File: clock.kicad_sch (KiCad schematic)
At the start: 52 parts, among them J1 USB_C_Receptacle_USB2.0_16P, J3 Conn_01x02_Pin, J4 Conn_01x02_Pin, J5 Battery, Q1 NMOS-SI2302, Q2 NPN, SW1 SW_SPST, SW2 SW_SPST, SW4 SW_SPDT, SW5 SW_SPST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

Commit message: changed it ig
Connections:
- net +3.3V: now also BZ1.1 (+)
- net BUZZER: now also R13.1; no longer BZ1.1 (+)
- net GND: now also Q2.3 (E); no longer BZ1.2 (-)
- net at D1.2 (A), Q2.1 (C): now also BZ1.2 (-)
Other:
- moved on the sheet: BZ1
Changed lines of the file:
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@@
 	(global_label "BUZZER"
 		(shape input)
-		(at 257.81 87.63 180)
+		(at 224.79 90.17 180)
 		(fields_autoplaced yes)
 		(effects
@@
 		)
 		(property "Intersheetrefs" "${INTERSHEET_REFS}"
-			(at 247.3863 87.63 0)
+			(at 214.3663 90.17 0)
 			(effects
 				(font
@@
 	(symbol
 		(lib_id "Device:Buzzer")
-		(at 260.35 90.17 0)
+		(at 246.38 81.28 0)
 		(unit 1)
 		(exclude_from_sim no)
@@
 		(fields_autoplaced yes)
 		(property "Reference" "BZ1"
-			(at 264.16 88.8999 0)
+			(at 250.19 80.0099 0)
 			(effects
 				(font
@@
 		)
 		(property "Value" "Buzzer"
-			(at 264.16 91.4399 0)
+			(at 250.19 82.5499 0)
 			(effects
 				(font
@@
 		)
 		(property "Footprint" "Buzzer_Beeper:MagneticBuzzer_CUI_CMT-8504-100-SMT"
-			(at 259.715 87.63 90)
+			(at 245.745 78.74 90)
 			(effects
 				(font
@@
 		)
 		(property "Datasheet" "~"
-			(at 259.715 87.63 90)
+			(at 245.745 78.74 90)
 			(effects
 				(font
@@
 		)
 		(property "Description" "Buzzer, polarized"
-			(at 260.35 90.17 0)
+			(at 246.38 81.28 0)
 			(effects
 				(font
@@
 	(symbol
 		(lib_id "power:GND")
-		(at 257.81 92.71 270)
+		(at 240.03 95.25 0)
 		(unit 1)
 		(exclude_from_sim no)
@@
 		(fields_autoplaced yes)
 		(property "Reference" "#PWR09"
-			(at 251.46 92.71 0)
+			(at 240.03 101.6 0)
 			(effects
 				(font
@@
 		)
 		(property "Value" "GND"
-			(at 256.54 88.9 90)
+			(at 242.57 96.5199 0)
 			(effects
 				(font
 					(size 1.27 1.27)
 				)
+				(justify left)
 			)
 		)
 		(property "Footprint" ""
-			(at 257.81 92.71 0)
+			(at 240.03 95.25 0)
 			(effects
 				(font
@@
 		)
 		(property "Datasheet" ""
-			(at 257.81 92.71 0)
+			(at 240.03 95.25 0)
 			(effects
 				(font
@@
 		)
 		(property "Description" "Power symbol creates a global label with name \"GND\" , ground"
-			(at 257.81 92.71 0)
+			(at 240.03 95.25 0)
 			(effects
 				(font

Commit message: idk again
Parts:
- R13: value 470R -> 180R
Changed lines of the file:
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@@
 			)
 		)
-		(property "Value" "470R"
+		(property "Value" "180R"
 			(at 228.6 86.36 90)
 			(effects

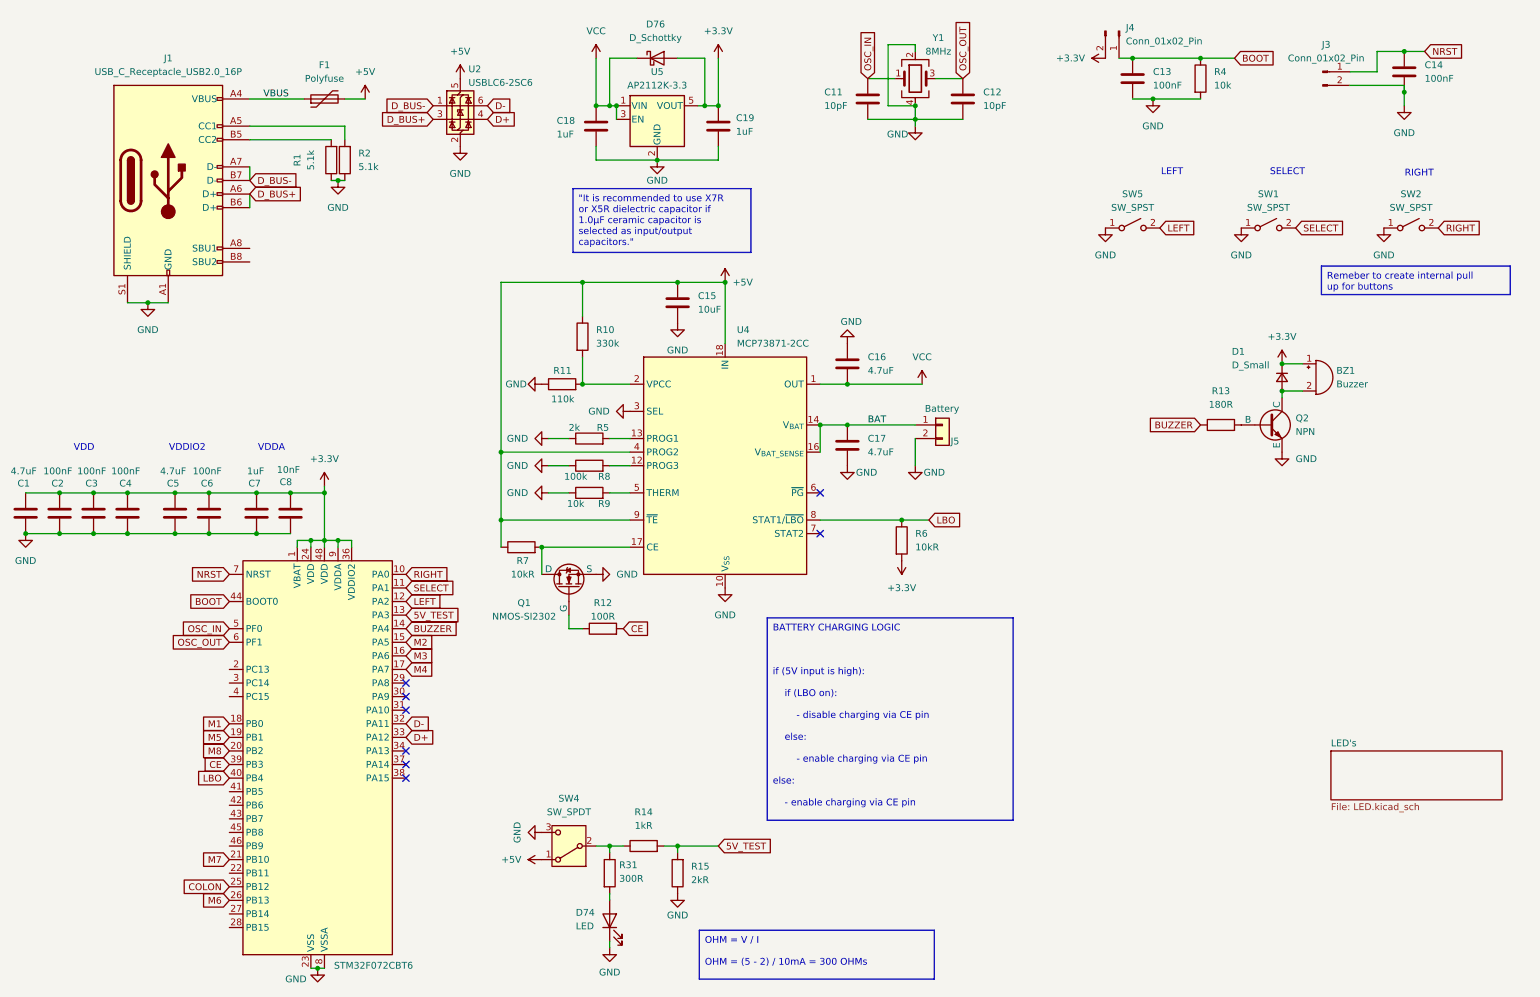
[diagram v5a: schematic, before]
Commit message: looking good, changed buzzer, changed buzzer pin, changed resistors, changed stcube ide config
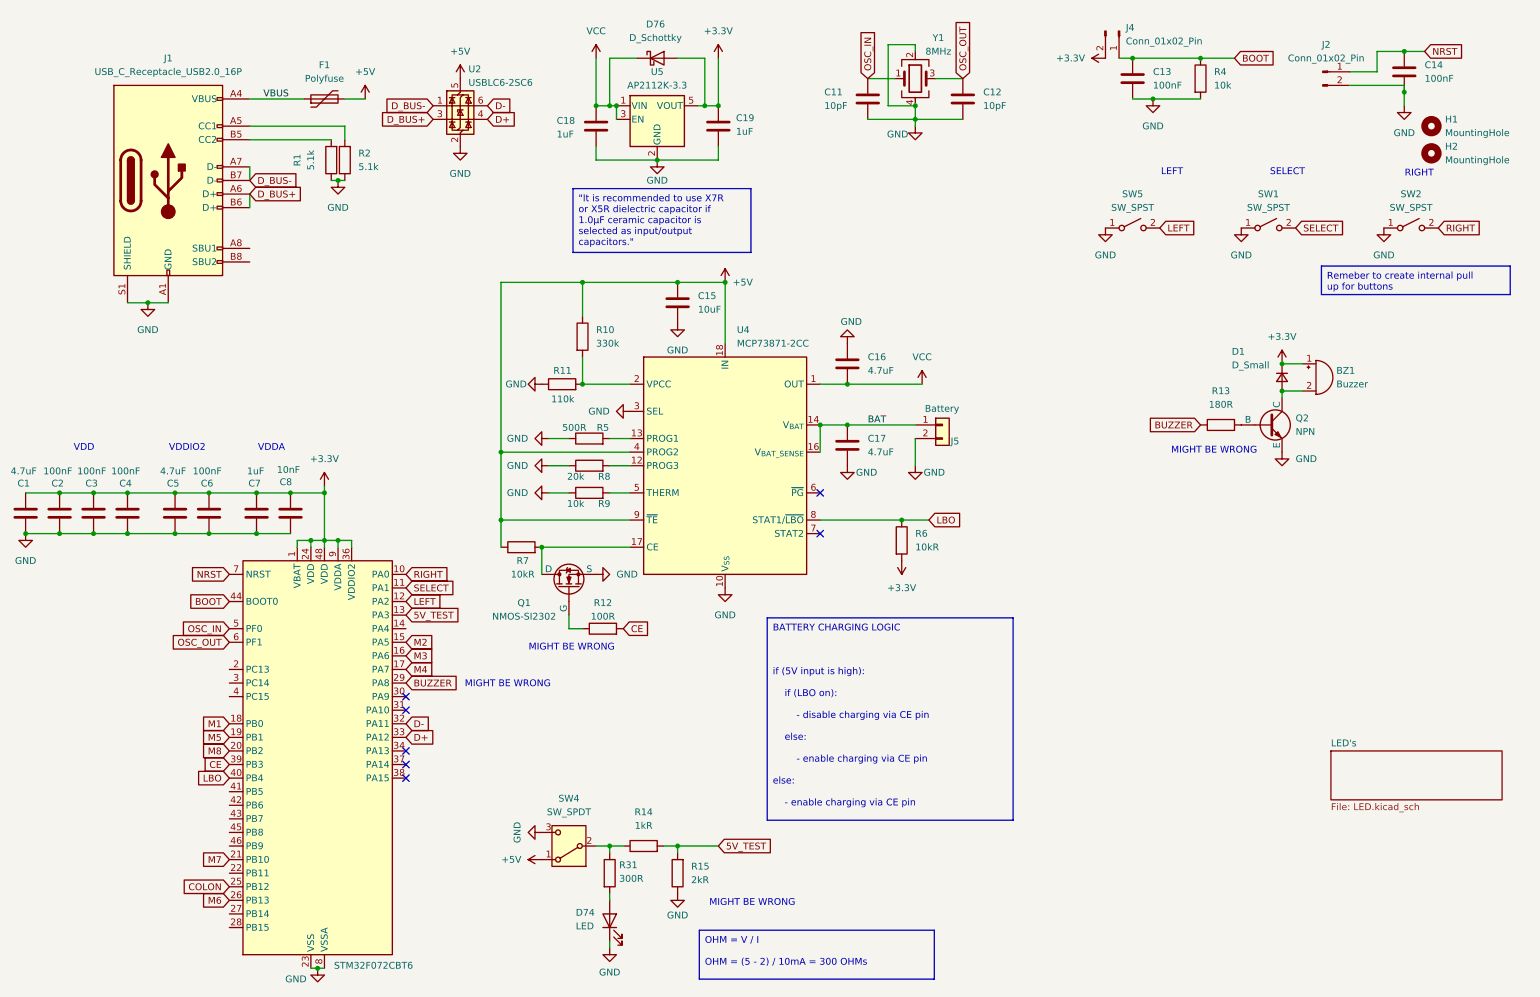
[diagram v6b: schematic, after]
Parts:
- removed J3: Conn_01x02_Pin, Connector_PinHeader_2.54mm:PinHeader_1x02_P2.54mm_Vertical, symbol Connector:Conn_01x02_Pin
- added H1, H2: MountingHole, MountingHole:MountingHole_3.2mm_M3, symbol Mechanical:MountingHole
- added J2: Conn_01x02_Pin, Connector_PinHeader_2.54mm:PinHeader_1x02_P2.54mm_Vertical, symbol Connector:Conn_01x02_Pin
- BZ1: footprint Buzzer_Beeper:MagneticBuzzer_CUI_CMT-8504-100-SMT -> FB_clock_lib:Buzzer
- R5: value 2k -> 500R
- R8: value 100k -> 20k
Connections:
- net BUZZER: now also U1.29 (PA8); no longer U1.14 (PA4)
- net GND: now also J2.2 (Pin_2)
- net NRST: now also J2.1 (Pin_1)
- no-connect marks 8 -> 7
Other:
- note added: "MIGHT BE WRONG"
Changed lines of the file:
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@@
 	)
 	(no_connect
-		(at 76.2 138.43)
-	)
-	(no_connect
 		(at 76.2 140.97)
 	)
@@
 		)
 	)
+	(text "MIGHT BE WRONG\n"
+		(exclude_from_sim no)
+		(at 227.33 94.996 0)
+		(effects
+			(font
+				(size 1.27 1.27)
+			)
+		)
+	)
 	(text "VDDA"
 		(exclude_from_sim no)
@@
 		)
 	)
+	(text "MIGHT BE WRONG\n"
+		(exclude_from_sim no)
+		(at 95.25 138.684 0)
+		(effects
+			(font
+				(size 1.27 1.27)
+			)
+		)
+	)
+	(text "MIGHT BE WRONG\n"
+		(exclude_from_sim no)
+		(at 140.97 179.578 0)
+		(effects
+			(font
+				(size 1.27 1.27)
+			)
+		)
+	)
 	(text "RIGHT"
 		(exclude_from_sim no)
@@
 		)
 	)
+	(text "MIGHT BE WRONG\n"
+		(exclude_from_sim no)
+		(at 107.188 131.826 0)
+		(effects
+			(font
+				(size 1.27 1.27)
+			)
+		)
+	)
 	(label "BAT"
 		(at 162.56 90.17 0)
-		(fields_autoplaced yes)
 		(effects
 			(font
@@
 	(label "VBUS"
 		(at 49.53 29.21 0)
-		(fields_autoplaced yes)
 		(effects
 			(font
@@
 	(global_label "BUZZER"
 		(shape input)
-		(at 76.2 128.27 0)
+		(at 76.2 138.43 0)
 		(fields_autoplaced yes)
 		(effects
@@
 		)
 		(property "Intersheetrefs" "${INTERSHEET_REFS}"
-			(at 86.6237 128.27 0)
+			(at 86.6237 138.43 0)
 			(effects
 				(font
@@
 			)
 		)
-		(property "Footprint" "Buzzer_Beeper:MagneticBuzzer_CUI_CMT-8504-100-SMT"
+		(property "Footprint" "FB_clock_lib:Buzzer"
 			(at 245.745 78.74 90)
 			(effects
@@
 			)
 		)
-		(property "Value" "2k"
+		(property "Value" "500R"
 			(at 107.696 90.678 90)
 			(effects
@@
 	)
 	(symbol
+		(lib_id "Connector:Conn_01x02_Pin")
+		(at 247.65 24.13 0)
+		(unit 1)
+		(exclude_from_sim no)
+		(in_bom yes)
+		(on_board yes)
+		(dnp no)
+		(fields_autoplaced yes)
+		(property "Reference" "J2"
+			(at 248.285 19.05 0)
+			(effects
+				(font
+					(size 1.27 1.27)
+				)
+			)
+		)
+		(property "Value" "Conn_01x02_Pin"
+			(at 248.285 21.59 0)
+			(effects
+				(font
+					(size 1.27 1.27)
+				)
+			)
+		)
+		(property "Footprint" "Connector_PinHeader_2.54mm:PinHeader_1x02_P2.54mm_Vertical"
+			(at 247.65 24.13 0)
+			(effects
+				(font
+					(size 1.27 1.27)
+				)
+				(hide yes)
+			)
+		)
+		(property "Datasheet" "~"
+			(at 247.65 24.13 0)
+			(effects
+				(font
+					(size 1.27 1.27)
+				)
+				(hide yes)
+			)
+		)
+		(property "Description" "Generic connector, single row, 01x02, script generated"
+			(at 247.65 24.13 0)
+			(effects
+				(font
+					(size 1.27 1.27)
+				)
+				(hide yes)
+			)
+		)
+		(pin "2"
+		)
+		(pin "1"
+		)
+		(instances
+			(project "clock"
+				(path "/959d2641-02eb-4caa-b1c6-84a86321825f"
+					(reference "J2")
+					(unit 1)
+				)
+			)
+		)
+	)
+	(symbol
 		(lib_id "Device:R")
 		(at 62.23 40.64 180)
@@
 			)
 		)
-		(property "Value" "100k"
+		(property "Value" "20k"
 			(at 107.95 99.822 90)
 			(effects
@@
 	)
 	(symbol
-		(lib_id "Connector:Conn_01x02_Pin")
-		(at 247.65 24.13 0)
-		(unit 1)
-		(exclude_from_sim no)
-		(in_bom yes)
-		(on_board yes)
-		(dnp no)
-		(fields_autoplaced yes)
-		(property "Reference" "J3"
-			(at 248.285 19.05 0)
-			(effects
-				(font
-					(size 1.27 1.27)
-				)
-			)
-		)
-		(property "Value" "Conn_01x02_Pin"
-			(at 248.285 21.59 0)
-			(effects
-				(font
-					(size 1.27 1.27)
-				)
-			)
-		)
-		(property "Footprint" "Connector_PinHeader_2.54mm:PinHeader_1x02_P2.54mm_Vertical"
-			(at 247.65 24.13 0)
-			(effects
-				(font
-					(size 1.27 1.27)
-				)
-				(hide yes)
-			)
-		)
-		(property "Datasheet" "~"
-			(at 247.65 24.13 0)
-			(effects
-				(font
-					(size 1.27 1.27)
-				)
-				(hide yes)
-			)
-		)
-		(property "Description" "Generic connector, single row, 01x02, script generated"
-			(at 247.65 24.13 0)
-			(effects
-				(font
-					(size 1.27 1.27)
-				)
-				(hide yes)
-			)
-		)
-		(pin "2"
-		)
-		(pin "1"
-		)
-		(instances
-			(project "clock"
-				(path "/959d2641-02eb-4caa-b1c6-84a86321825f"
-					(reference "J3")
-					(unit 1)
-				)
-			)
-		)
-	)
-	(symbol
 		(lib_id "Switch:SW_SPDT")
 		(at 106.68 168.91 180)
@@
 	)
 	(symbol
+		(lib_id "Mechanical:MountingHole")
+		(at 267.97 39.37 0)
+		(unit 1)
+		(exclude_from_sim yes)
+		(in_bom no)
+		(on_board yes)
+		(dnp no)
+		(fields_autoplaced yes)
+		(property "Reference" "H2"
+			(at 270.51 38.0999 0)
+			(effects
+				(font
+					(size 1.27 1.27)
+				)
+				(justify left)
+			)
+		)
+		(property "Value" "MountingHole"
+			(at 270.51 40.6399 0)
+			(effects
+				(font
+					(size 1.27 1.27)
+				)
+				(justify left)
+			)
+		)
+		(property "Footprint" "MountingHole:MountingHole_3.2mm_M3"
+			(at 267.97 39.37 0)
+			(effects
+				(font
+					(size 1.27 1.27)
+				)
+				(hide yes)
+			)
+		)
+		(property "Datasheet" "~"
+			(at 267.97 39.37 0)
+			(effects
+				(font
+					(size 1.27 1.27)
+				)
+				(hide yes)
+			)
+		)
+		(property "Description" "Mounting Hole without connection"
+			(at 267.97 39.37 0)
+			(effects
+				(font
+					(size 1.27 1.27)
+				)
+				(hide yes)
+			)
+		)
+		(instances
+			(project "clock"
+				(path "/959d2641-02eb-4caa-b1c6-84a86321825f"
+					(reference "H2")
+					(unit 1)
+				)
+			)
+		)
+	)
+	(symbol
 		(lib_id "power:GND")
 		(at 127 71.12 0)
@@
 					(unit 1)
 				)
+			)
+		)
+	)
+	(symbol
+		(lib_id "Mechanical:MountingHole")
+		(at 267.97 34.29 0)
+		(unit 1)
+		(exclude_from_sim yes)
+		(in_bom no)
+		(on_board yes)
+		(dnp no)
+		(fields_autoplaced yes)
+		(property "Reference" "H1"
+			(at 270.51 33.0199 0)
+			(effects
+				(font
+					(size 1.27 1.27)
+				)
+				(justify left)
+			)
+		)
+		(property "Value" "MountingHole"
+			(at 270.51 35.5599 0)
+			(effects
+				(font
+					(size 1.27 1.27)
+				)
+				(justify left)
+			)
+		)
+		(property "Footprint" "MountingHole:MountingHole_3.2mm_M3"
+			(at 267.97 34.29 0)
+			(effects
+				(font
+					(size 1.27 1.27)
+				)
+				(hide yes)
+			)
+		)
+		(property "Datasheet" "~"
+			(at 267.97 34.29 0)
+			(effects
+				(font
+					(size 1.27 1.27)
+				)
+				(hide yes)
+			)
+		)
+		(property "Description" "Mounting Hole without connection"
+			(at 267.97 34.29 0)
+			(effects
+				(font
+					(size 1.27 1.27)
+				)
+				(hide yes)
+			)
+		)
+		(instances
+			(project ""
+				(path "/959d2641-02eb-4caa-b1c6-84a86321825f"
+					(reference "H1")
+					(unit 1)
+				)

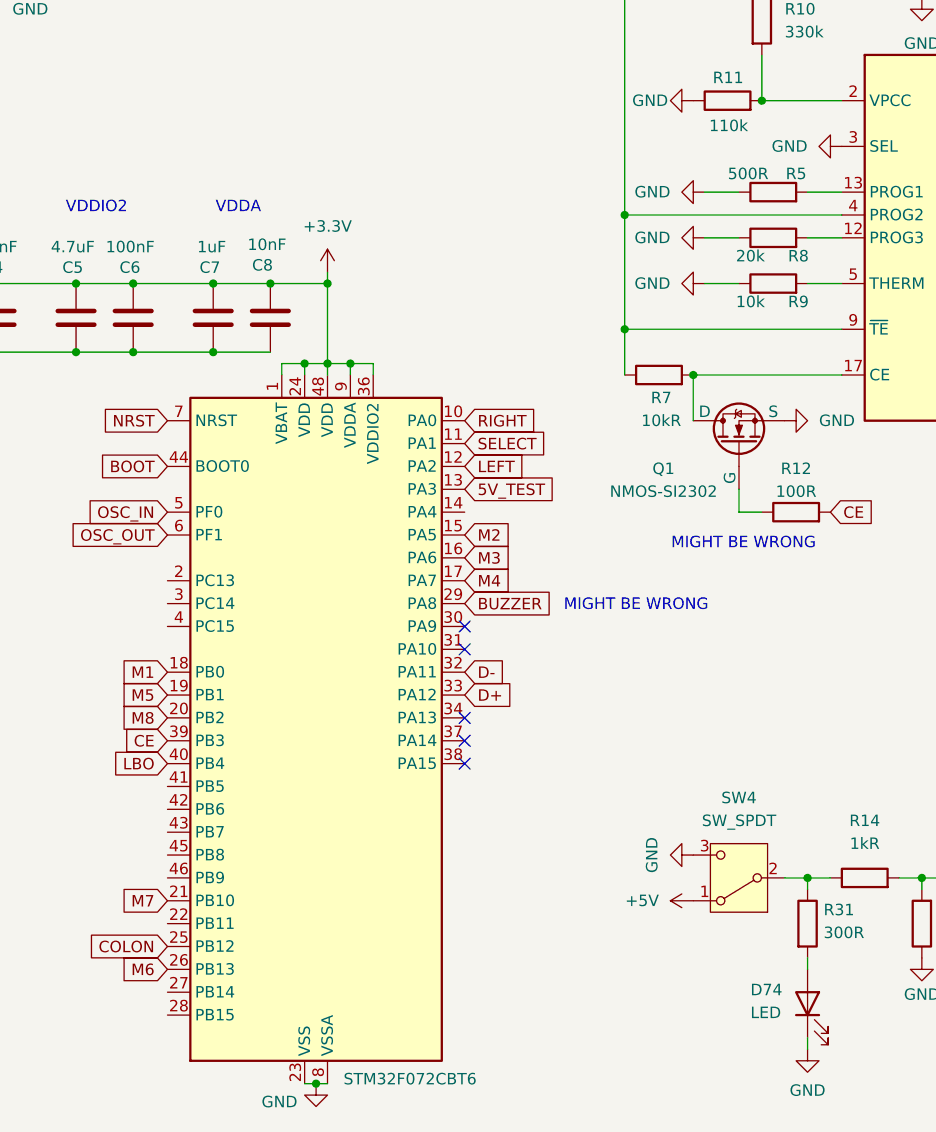
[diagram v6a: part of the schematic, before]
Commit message: changed resistor values
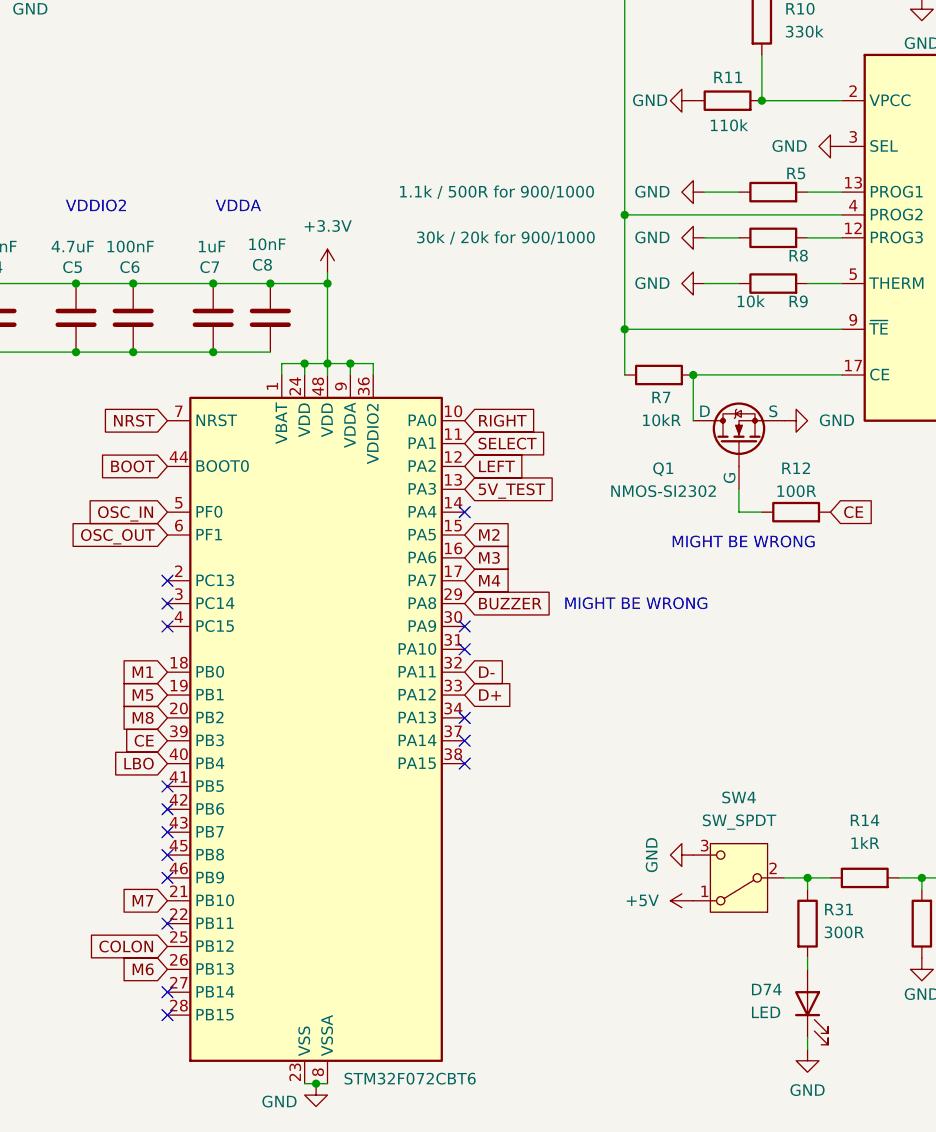
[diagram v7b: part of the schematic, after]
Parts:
- R5: value 500R -> 1.1k / 500R for 900/1000
- R8: value 20k -> 30k / 20k for 900/1000
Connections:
- no-connect marks 7 -> 19
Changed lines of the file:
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@@
 	)
 	(no_connect
+		(at 43.18 163.83)
+	)
+	(no_connect
 		(at 153.67 102.87)
 	)
 	(no_connect
+		(at 43.18 140.97)
+	)
+	(no_connect
 		(at 76.2 156.21)
 	)
 	(no_connect
+		(at 43.18 184.15)
+	)
+	(no_connect
 		(at 76.2 153.67)
 	)
 	(no_connect
+		(at 43.18 138.43)
+	)
+	(no_connect
+		(at 43.18 173.99)
+	)
+	(no_connect
 		(at 153.67 110.49)
 	)
 	(no_connect
+		(at 43.18 135.89)
+	)
+	(no_connect
+		(at 43.18 161.29)
+	)
+	(no_connect
+		(at 43.18 166.37)
+	)
+	(no_connect
 		(at 76.2 140.97)
 	)
+	(no_connect
+		(at 43.18 168.91)
+	)
+	(no_connect
+		(at 43.18 181.61)
+	)
+	(no_connect
+		(at 76.2 128.27)
+	)
+	(no_connect
+		(at 43.18 158.75)
+	)
 	(wire
 		(pts
@@
 	(label "BAT"
 		(at 162.56 90.17 0)
+		(fields_autoplaced yes)
 		(effects
 			(font
@@
 	(label "VBUS"
 		(at 49.53 29.21 0)
+		(fields_autoplaced yes)
 		(effects
 			(font
@@
 			)
 		)
-		(property "Value" "500R"
-			(at 107.696 90.678 90)
+		(property "Value" "1.1k / 500R for 900/1000"
+			(at 79.756 92.71 90)
 			(effects
 				(font
@@
 			)
 		)
-		(property "Value" "20k"
-			(at 107.95 99.822 90)
+		(property "Value" "30k / 20k for 900/1000"
+			(at 80.772 97.79 90)
 			(effects
 				(font
